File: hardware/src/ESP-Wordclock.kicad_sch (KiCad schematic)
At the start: 1 part

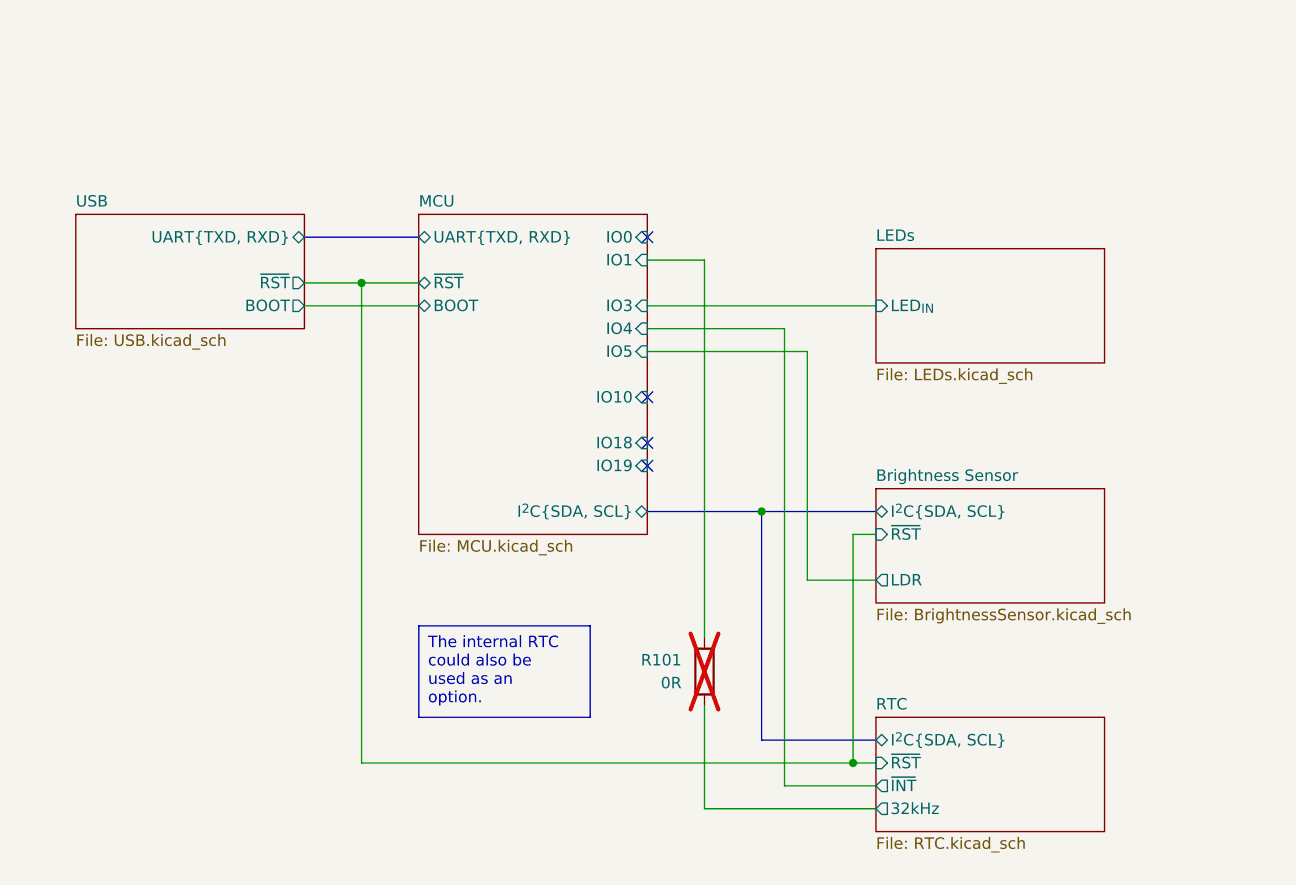
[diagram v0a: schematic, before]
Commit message: Add: Alternative USB connection, directly to the ESP USB_DP and USB_DN
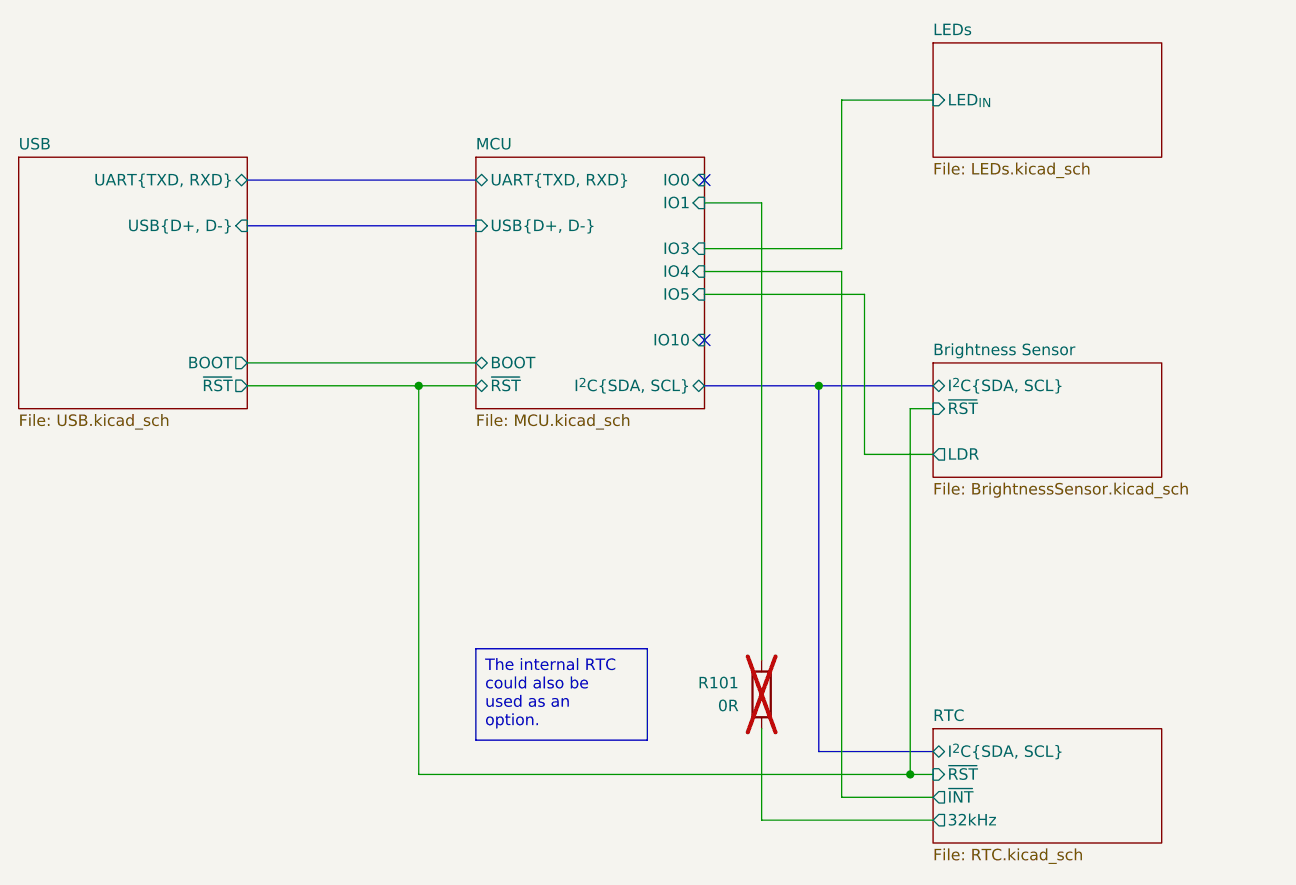
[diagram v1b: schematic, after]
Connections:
- no-connect marks 4 -> 2
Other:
- sheet MCU ports: added USB{D+, D-}; removed IO18, IO19
- sheet USB ports: added USB{D+, D-}; removed none
- moved on the sheet: R101
